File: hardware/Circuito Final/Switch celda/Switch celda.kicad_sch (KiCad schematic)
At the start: 25 parts, among them Q1 MMBT2222A, Q2 MMBT2907A, Q3 MMBT2222A

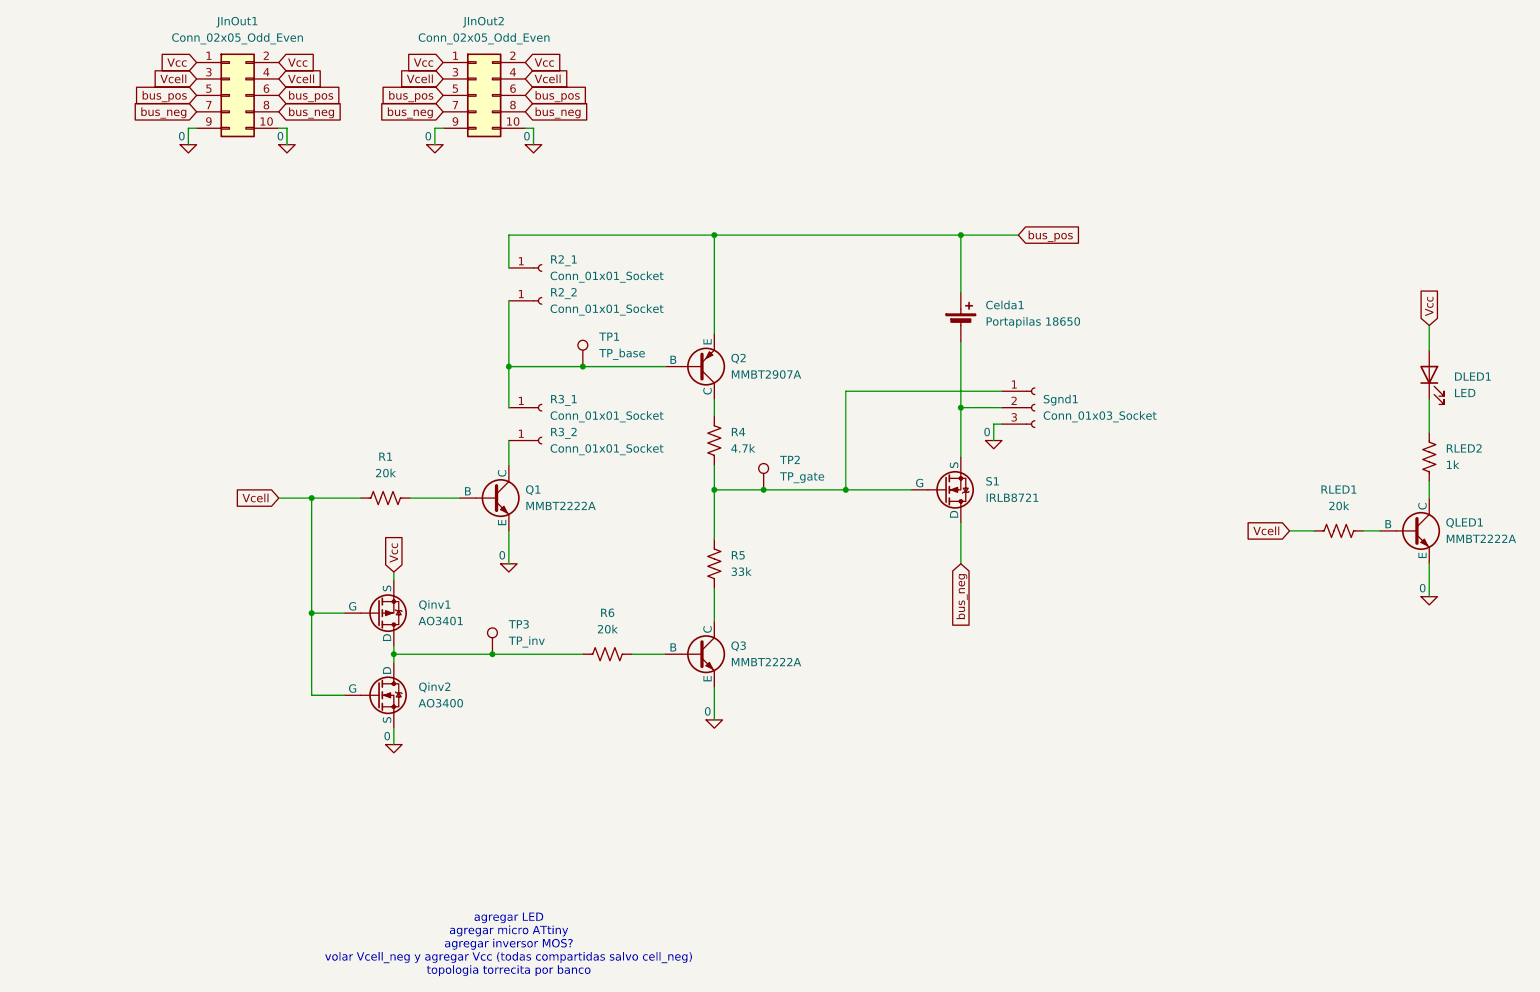
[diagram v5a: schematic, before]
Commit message: Finalización del esquemático de la celda y subida de datasheets nuevas
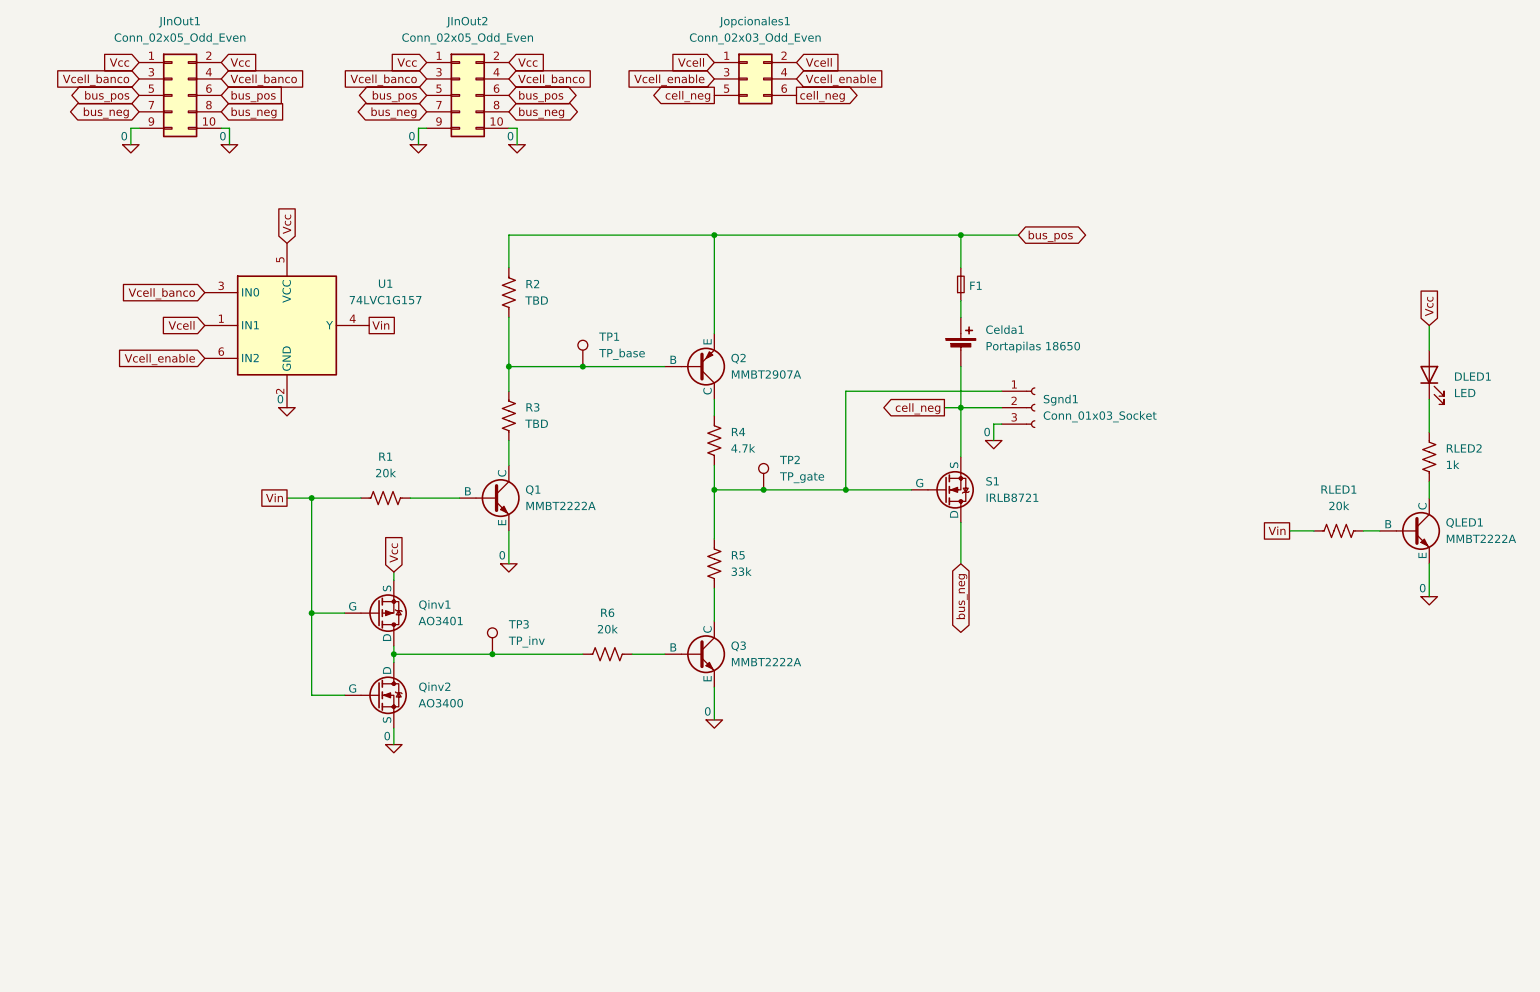
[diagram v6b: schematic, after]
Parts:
- removed R2_1, R2_2, R3_1, R3_2: Conn_01x01_Socket, Connector_PinSocket_2.54mm:PinSocket_1x01_P2.54mm_Vertical, symbol Connector:Conn_01x01_Socket
- added F1: ~, Fuse:Fuse_0603_1608Metric_Pad1.05x0.95mm_HandSolder, symbol Device:Fuse_Small
- added Jopcionales1: Conn_02x03_Odd_Even, Connector_PinHeader_2.54mm:PinHeader_2x03_P2.54mm_Horizontal, symbol Connector_Generic:Conn_02x03_Odd_Even
- added R2, R3: TBD, Resistor_SMD:R_0603_1608Metric_Pad0.98x0.95mm_HandSolder, symbol Device:R_US
- added U1: 74LVC1G157, Package_TO_SOT_SMD:SOT-363_SC-70-6_Handsoldering, symbol 74xGxx:74LVC1G57
- Celda1: footprint (none) -> Battery:BatteryHolder_MPD_BK-18650-PC2
- DLED1: footprint (none) -> LED_THT:LED_D5.0mm
- JInOut1: footprint (none) -> Connector_PinHeader_2.54mm:PinHeader_2x05_P2.54mm_Horizontal
- JInOut2: footprint (none) -> Connector_PinSocket_2.54mm:PinSocket_2x05_P2.54mm_Horizontal
- Q1, Q2, Q3, QLED1: footprint Package_TO_SOT_SMD:SOT-23-3 -> Package_TO_SOT_SMD:SOT-23_Handsoldering
- Qinv1, Qinv2: footprint (none) -> Package_TO_SOT_SMD:SOT-23_Handsoldering
- TP1, TP2, TP3: footprint TestPoint:TestPoint_Bridge_Pitch2.54mm_Drill1.0mm -> TestPoint:TestPoint_Loop_D2.54mm_Drill1.5mm_Beaded
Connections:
- net 0: now also U1.2 (GND)
- net Vcc: now also U1.5 (VCC)
- net Vcell: now also Jopcionales1.1 (Pin_1), Jopcionales1.2 (Pin_2), U1.1 (IN1); no longer JInOut1.3 (Pin_3), JInOut1.4 (Pin_4), JInOut2.3 (Pin_3), JInOut2.4 (Pin_4), Qinv1.2 (G), Qinv2.2 (G), R1.1, RLED1.1
- net bus_pos: now also F1.2, R2.2; no longer Celda1.1 (+)
- net cell_neg: now reaches Celda1.2 (-), S1.3 (S), Sgnd1.2 (Pin_2)
- net cell_neg: now also Jopcionales1.5 (Pin_5), Jopcionales1.6 (Pin_6)
- net at Q2.2 (B), TP1.1: now also R2.1, R3.2
- net at Q1.1 (C): now also R3.1
- new net: Celda1.1 (+), F1.1
- new net Vcell_banco: JInOut1.3 (Pin_3), JInOut1.4 (Pin_4), JInOut2.3 (Pin_3), JInOut2.4 (Pin_4), U1.3 (IN0)
- new net Vcell_enable: Jopcionales1.3 (Pin_3), Jopcionales1.4 (Pin_4), U1.6 (IN2)
- new net Vin: Qinv1.2 (G), Qinv2.2 (G), R1.1, RLED1.1, U1.4 (Y)
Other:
- note removed: "agregar LED agregar micro ATtiny agregar inversor MOS? volar Vcell_neg y agregar Vcc (todas compartidas salvo cell_neg) topologia torrecita por banco"
- moved on the sheet: Celda1, JInOut1, JInOut2

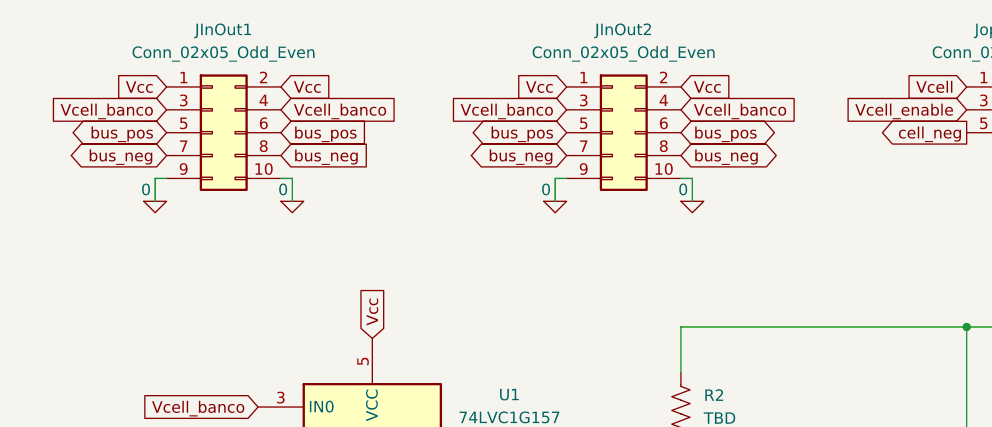
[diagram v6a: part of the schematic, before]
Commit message: Update PCB celda completo - Revisar integridad
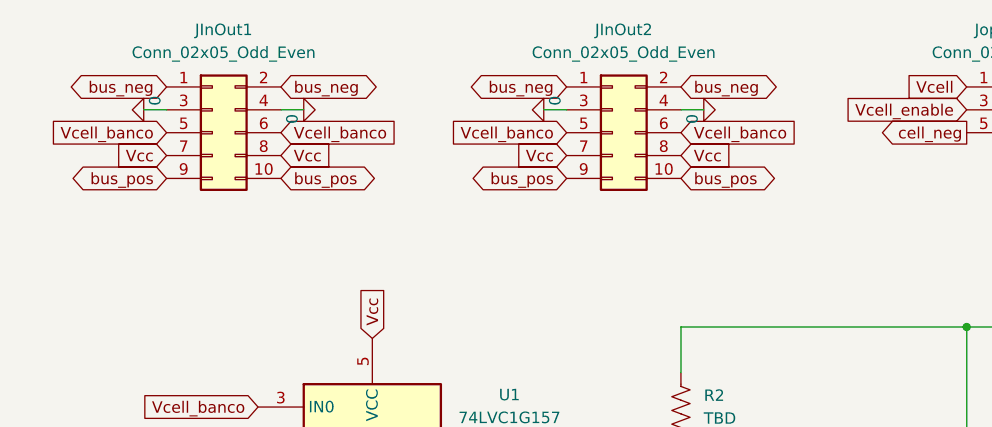
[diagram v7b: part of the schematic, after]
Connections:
- net 0: now also JInOut1.3 (Pin_3), JInOut1.4 (Pin_4), JInOut2.3 (Pin_3), JInOut2.4 (Pin_4); no longer JInOut1.10 (Pin_10), JInOut1.9 (Pin_9), JInOut2.10 (Pin_10), JInOut2.9 (Pin_9)
- net Vcc: now also JInOut1.7 (Pin_7), JInOut1.8 (Pin_8), JInOut2.7 (Pin_7), JInOut2.8 (Pin_8); no longer JInOut1.1 (Pin_1), JInOut1.2 (Pin_2), JInOut2.1 (Pin_1), JInOut2.2 (Pin_2)
- net Vcell_banco: now also JInOut1.5 (Pin_5), JInOut1.6 (Pin_6), JInOut2.5 (Pin_5), JInOut2.6 (Pin_6); no longer JInOut1.3 (Pin_3), JInOut1.4 (Pin_4), JInOut2.3 (Pin_3), JInOut2.4 (Pin_4)
- net bus_neg: now also JInOut1.1 (Pin_1), JInOut1.2 (Pin_2), JInOut2.1 (Pin_1), JInOut2.2 (Pin_2); no longer JInOut1.7 (Pin_7), JInOut1.8 (Pin_8), JInOut2.7 (Pin_7), JInOut2.8 (Pin_8)
- net bus_pos: now also JInOut1.10 (Pin_10), JInOut1.9 (Pin_9), JInOut2.10 (Pin_10), JInOut2.9 (Pin_9); no longer JInOut1.5 (Pin_5), JInOut1.6 (Pin_6), JInOut2.5 (Pin_5), JInOut2.6 (Pin_6)
